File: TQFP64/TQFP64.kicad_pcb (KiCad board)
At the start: 2 copper layers, 81.5 x 20.6 mm, 12 parts, among them J1 Conn_01x32, J2 Conn_02x32_Counter_Clockwise, J3 Conn_02x32_Counter_Clockwise, J4 Conn_02x32_Counter_Clockwise, J5 Conn_01x32, J6 Conn_01x06

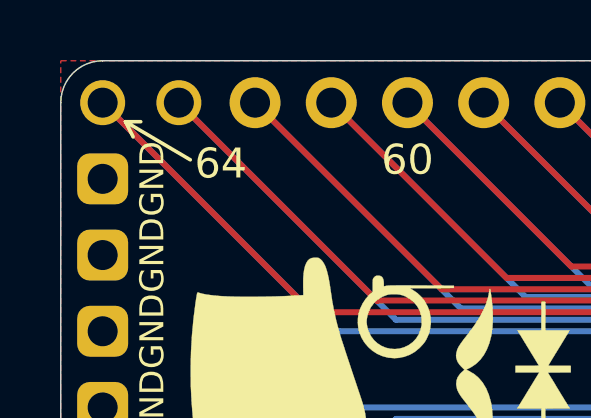
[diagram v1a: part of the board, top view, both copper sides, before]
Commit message: Silkscreen Edits
Dimensions moved to Drawings Layer
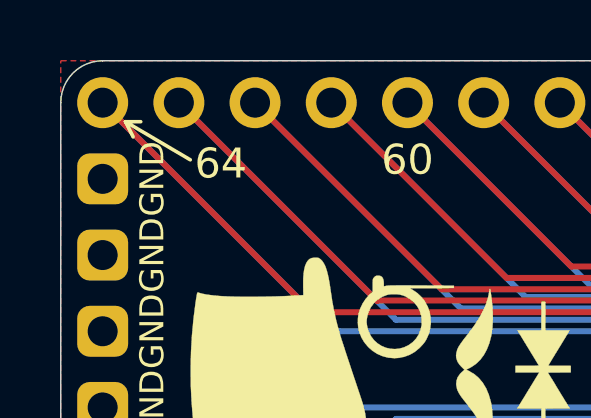
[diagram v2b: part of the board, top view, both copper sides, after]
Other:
- rule pad_to_mask_clearance: 0.051 -> 0
- rule solder_mask_min_width: 0.25 -> 0.1

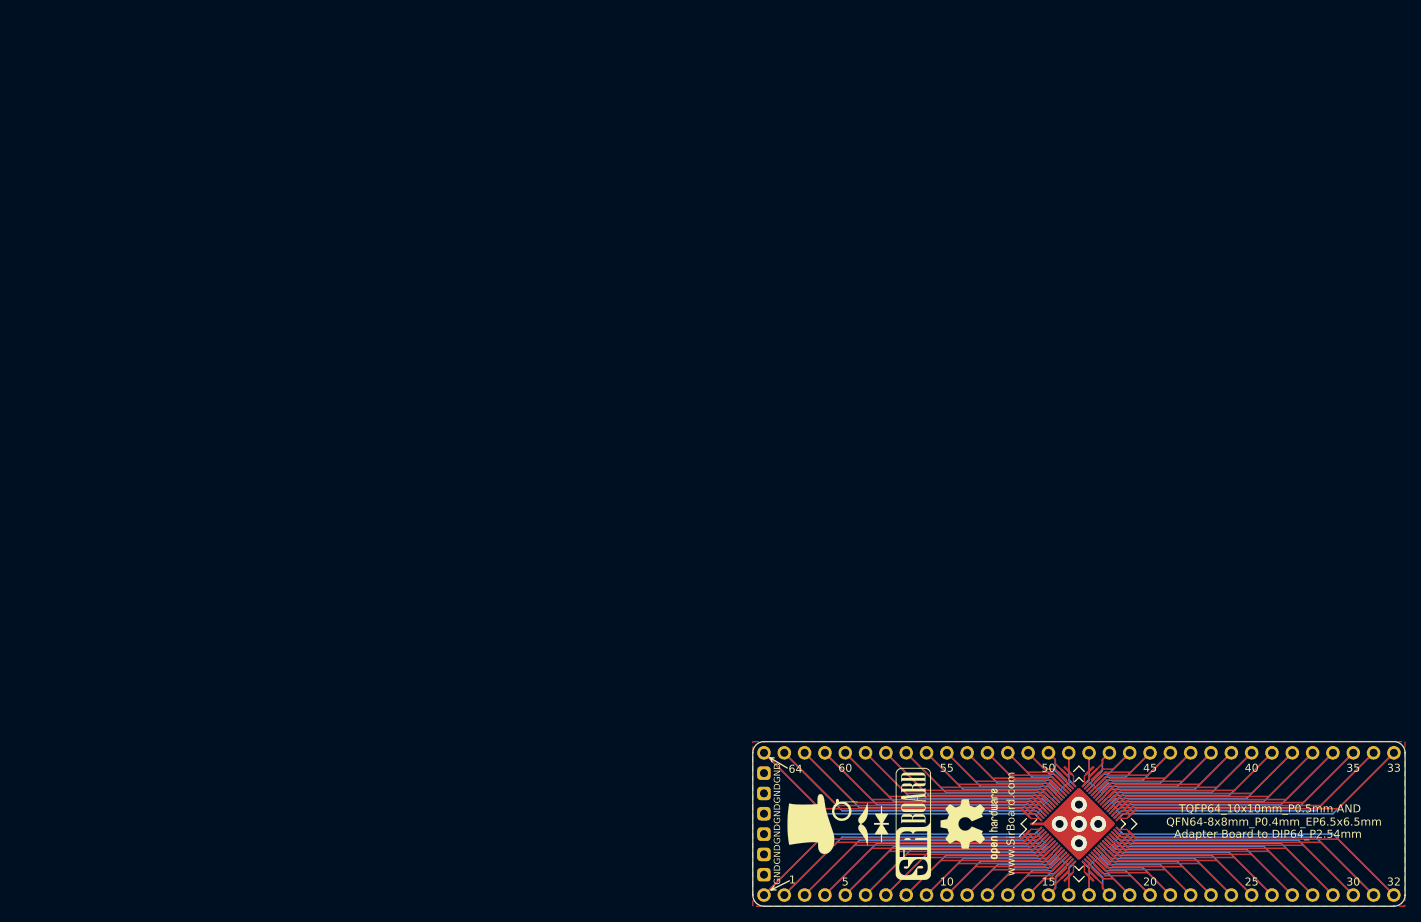
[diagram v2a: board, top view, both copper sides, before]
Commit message: USB, SD and CR Cells Added
MicroSD, MicroUSB, MiniUSB, USB-C, CR1220, CR2032 added as well as all schematics page sizes optimised
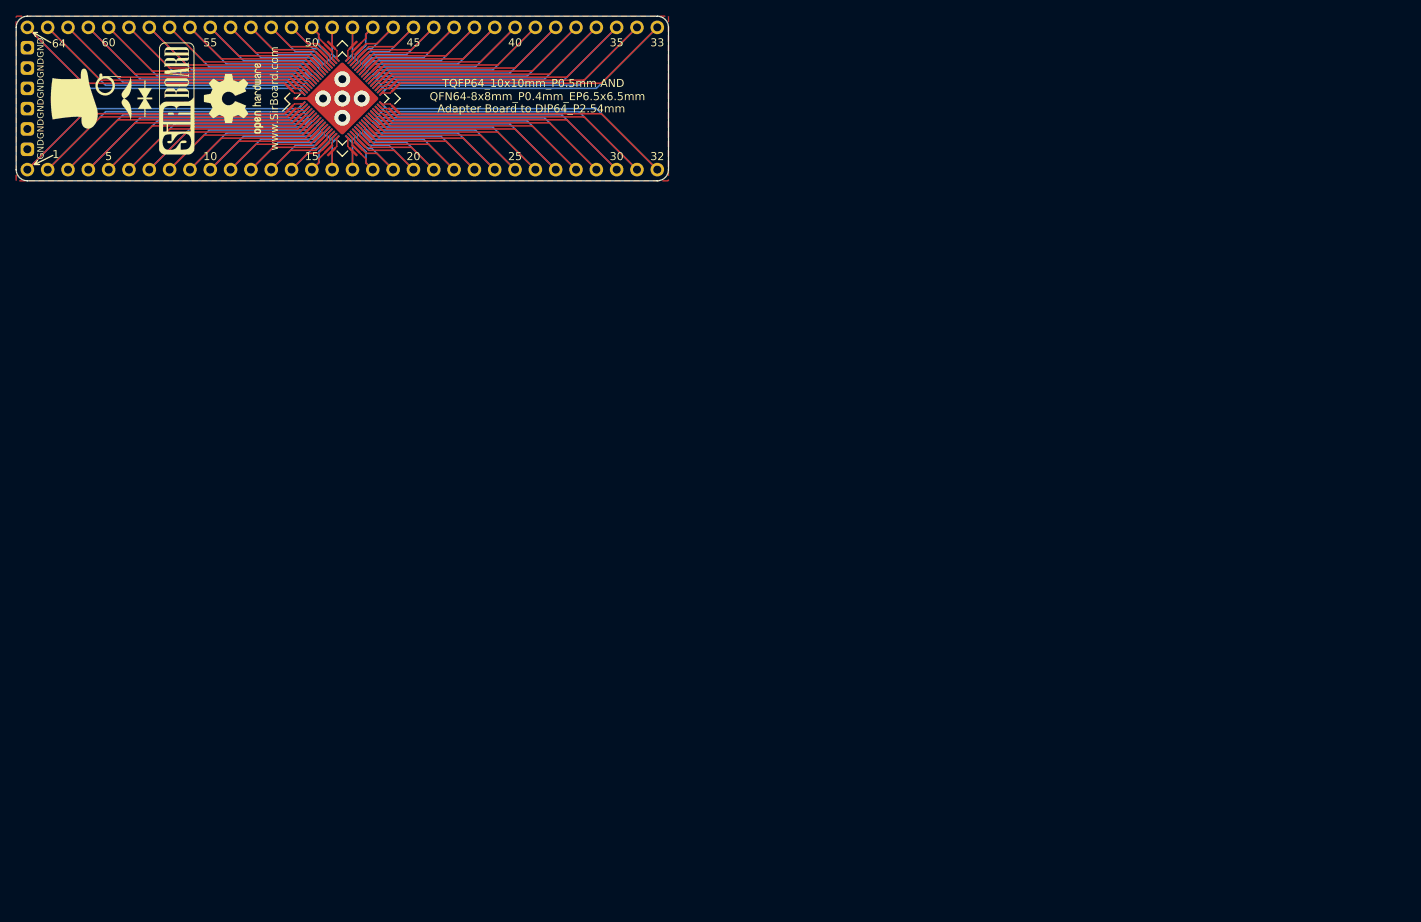
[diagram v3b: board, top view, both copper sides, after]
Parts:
- moved J1 129.2 mm to (29.0, 43.9)
- moved J2 129.2 mm to (68.3, 35.1)
- moved J3 129.2 mm to (68.3, 35.1)
- moved J4 129.2 mm to (68.3, 35.1)
- moved J5 129.2 mm to (29.0, 26.2)
- moved J6 129.2 mm to (29.0, 41.4)
- moved REF** 129.2 mm to (54.7, 35.1) (x2)
- moved G*** 129.2 mm to (38.2, 35.1) (x2)
- moved G*** 129.2 mm to (47.6, 35.1) (x2)

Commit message: Board Updates
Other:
- board size 81.5 x 20.6 mm -> 81.3 x 20.3 mm
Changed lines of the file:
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@@
     (35 F.Paste user hide)
     (36 B.SilkS user)
-    (37 F.SilkS user hide)
+    (37 F.SilkS user)
     (38 B.Mask user hide)
     (39 F.Mask user hide)
@@
     )
   )
+  (gr_line (start 108.966 43.942) (end 108.966 26.162) (layer Edge.Cuts) (width 0.05))
+  (gr_line (start 28.956 45.212) (end 107.696 45.212) (layer Edge.Cuts) (width 0.05))
+  (gr_line (start 27.686 26.162) (end 27.686 43.942) (layer Edge.Cuts) (width 0.05))
+  (gr_line (start 107.696 24.892) (end 28.956 24.892) (layer Edge.Cuts) (width 0.05))
+  (gr_arc (start 107.696 26.162) (end 108.966 26.162) (angle -90) (layer Edge.Cuts) (width 0.05))
+  (gr_arc (start 107.696 43.942) (end 107.696 45.212) (angle -90) (layer Edge.Cuts) (width 0.05))
+  (gr_arc (start 28.956 43.942) (end 27.686 43.942) (angle -90) (layer Edge.Cuts) (width 0.05))
+  (gr_arc (start 28.956 26.162) (end 28.956 24.892) (angle -90) (layer Edge.Cuts) (width 0.05))
   (gr_text "Adapter Board to DIP64_P2.54mm" (at 91.821 34.163 180) (layer B.SilkS)
     (effects (font (size 1 1) (thickness 0.15)) (justify mirror))
@@
     (arrow2b (pts (xy 27.559 19.939) (xy 28.685504 19.352579)))
   )
-  (gr_line (start 109.093 43.942) (end 109.093 26.162) (layer Edge.Cuts) (width 0.05))
-  (gr_line (start 28.956 45.339) (end 107.696 45.339) (layer Edge.Cuts) (width 0.05))
-  (gr_line (start 27.559 26.162) (end 27.559 43.942) (layer Edge.Cuts) (width 0.05))
-  (gr_line (start 107.696 24.765) (end 28.956 24.765) (layer Edge.Cuts) (width 0.05))
-  (gr_arc (start 107.696 26.162) (end 109.093 26.162) (angle -90) (layer Edge.Cuts) (width 0.05))
-  (gr_arc (start 107.696 43.942) (end 107.696 45.339) (angle -90) (layer Edge.Cuts) (width 0.05))
-  (gr_arc (start 28.956 43.942) (end 27.559 43.942) (angle -90) (layer Edge.Cuts) (width 0.05))
-  (gr_arc (start 28.956 26.162) (end 28.956 24.765) (angle -90) (layer Edge.Cuts) (width 0.05))
   (dimension 17.78 (width 0.12) (layer Dwgs.User)
     (gr_text "17.780 mm" (at 24.384 35.052 90) (layer Dwgs.User)
@@
     (polygon
       (pts
-        (xy 27.559 24.765) (xy 109.093 24.765) (xy 109.093 45.339) (xy 27.559 45.339)
+        (xy 27.686 24.892) (xy 108.966 24.892) (xy 108.966 45.212) (xy 27.686 45.212)
       )
     )

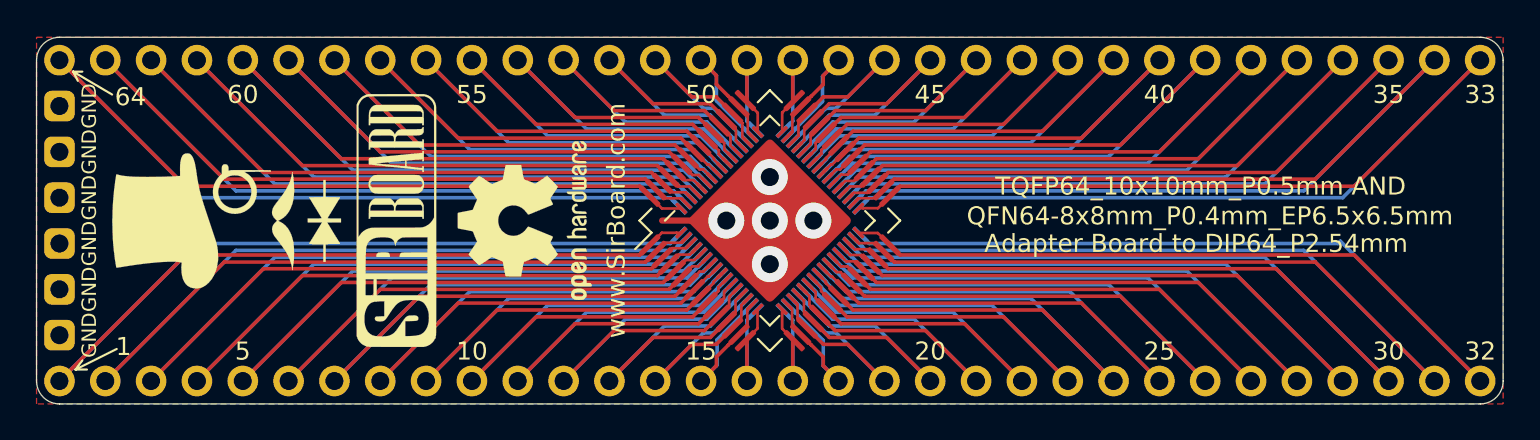
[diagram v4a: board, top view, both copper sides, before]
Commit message: Breakout Boards Revision 2
Renders updated, silkscreen text improved, blurry silkscreen items removed/resized.
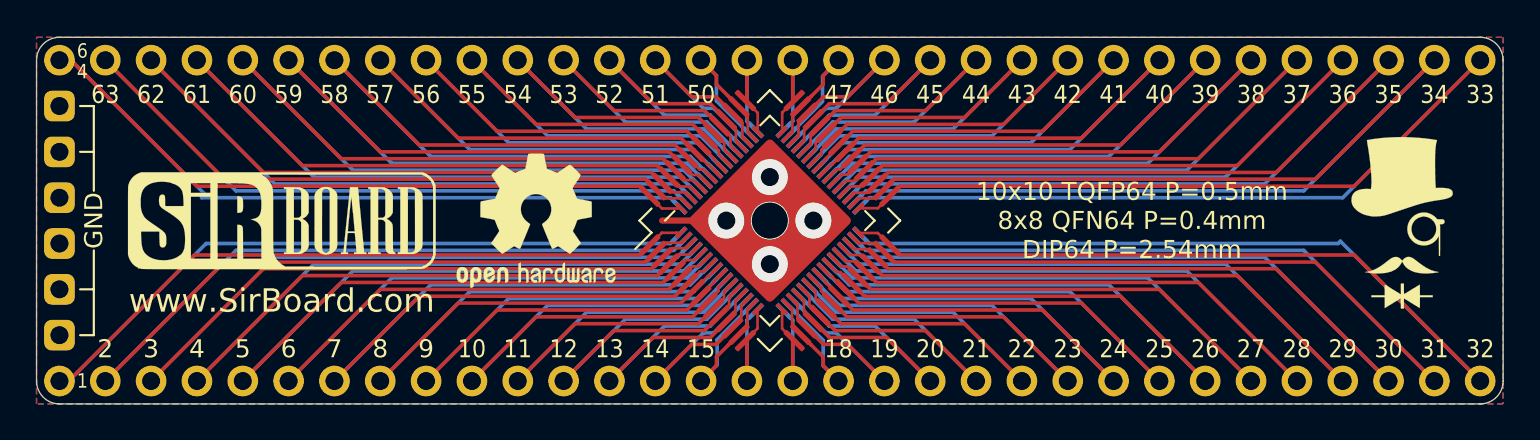
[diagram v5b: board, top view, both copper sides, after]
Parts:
- removed the G*** at (38.2, 35.1)
- removed the G*** at (47.6, 35.1)
- added G***: LOGO, logo:logo94x134, B.Cu at (103.4, 35.2)
- added G***: LOGO, logo:SirBoard171x54, B.Cu at (41.3, 35.1)
- G***: footprint logo:logo126x178 -> logo:logo94x134
- G***: footprint logo:SirBoard140x44 -> logo:SirBoard171x54
- moved G*** 65.2 mm to (103.4, 35.2), turned to 0 degrees
- moved G*** 6.35 mm to (41.3, 35.1), turned to 0 degrees
- moved REF** 0.63 mm to (55.4, 35.1), turned to 0 degrees (x2)
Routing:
- added copper zone on B.Cu, net Net-(J6-Pad1)
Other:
- board text added: "10x10 TQFP64 P=0.5mm 8x8 QFN64 P=0.4mm DIP64 P=2.54mm"
- board text added: "11"
- board text added: "12"
- board text added: "13"
- board text added: "14"
- board text added: "18"
- board text added: "19"
- board text added: "2"
- board text added: "21"
- board text added: "22"
- board text added: "23"
- board text added: "24"
- board text added: "26"
- board text added: "27"
- board text added: "28"
- board text added: "29"
- board text added: "3"
- board text added: "31"
- board text added: "34"
- board text added: "36"
- board text added: "37"
- board text added: "38"
- board text added: "39"
- board text added: "4"
- board text added: "41"
- board text added: "42"
- board text added: "43"
- board text added: "44"
- board text added: "46"
- board text added: "47"
- board text added: "51"
- board text added: "52"
- board text added: "53"
- board text added: "54"
- board text added: "56"
- board text added: "57"
- board text added: "58"
- board text added: "59"
- board text added: "6"
- board text added: "61"
- board text added: "62"
- board text added: "63"
- board text added: "7"
- board text added: "7x7 TQFP64 P=0.4mm 8x8 QFN64 P=0.4mm DIP64 P=2.54mm"
- board text added: "8"
- board text added: "9"
- board text removed: "64"
- board text removed: "Adapter Board to DIP64_P2.54mm"
- board text removed: "QFN64-8x8mm_P0.4mm_EP6.5x6.5mm"
- board text removed: "TQFP64_10x10mm_P0.5mm AND"
- board text removed: "TQFP64_7x7mm_P0.4mm"
